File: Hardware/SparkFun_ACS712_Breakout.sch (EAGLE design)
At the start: 12 parts, among them U1 ACS712

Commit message: A few more QC clean ups
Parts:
- added U$1: REVISION, SparkFun-Aesthetics:REVISION
- JP1, JP2: value M01-SMTSO-256-ET -> (none); device SparkFun:M01-SMTSO-256-ET -> SparkFun-Connectors:M01-SMTSO-256-ET
- JP3: device SparkFun:M04PTH -> SparkFun-Connectors:M04PTH
- JP4, JP5: device SparkFun:FIDUCIALUFIDUCIAL -> SparkFun-Aesthetics:FIDUCIALUFIDUCIAL
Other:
- note added: "P. Alberts, Toni Klopfenstein"
- note removed: "Revised by:Patrick Alberts"
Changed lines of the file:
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@@
 <?xml version="1.0" encoding="utf-8"?>
 <!DOCTYPE eagle SYSTEM "eagle.dtd">
-<eagle version="7.2.0">
+<eagle version="7.3.0">
 <drawing>
 <settings>
@@
 <layer number="113" name="IDFDebug" color="4" fill="1" visible="yes" active="yes"/>
 <layer number="116" name="Patch_BOT" color="9" fill="4" visible="no" active="yes"/>
+<layer number="118" name="Rect_Pads" color="7" fill="1" visible="yes" active="yes"/>
 <layer number="121" name="_tsilk" color="7" fill="1" visible="no" active="yes"/>
 <layer number="122" name="_bsilk" color="7" fill="1" visible="no" active="yes"/>
@@
 <layer number="255" name="routoute" color="7" fill="1" visible="yes" active="yes"/>
 </layers>
-<schematic xreflabel="%F%N/%S" xrefpart="/%S.%C%R">
+<schematic xreflabel="%F%N/%S" xrefpart="/%S">
 <attributes>
 </attributes>
@@
 <part name="U1" library="SparkFun-AnalogIC" deviceset="ACS712" device=""/>
 <part name="FRAME1" library="SparkFun-Aesthetics" deviceset="FRAME-LETTER" device=""/>
-<part name="JP1" library="SparkFun" deviceset="M01" device="-SMTSO-256-ET"/>
-<part name="JP2" library="SparkFun" deviceset="M01" device="-SMTSO-256-ET"/>
-<part name="JP3" library="SparkFun" deviceset="M04" device="PTH"/>
+<part name="JP1" library="SparkFun-Connectors" deviceset="M01" device="-SMTSO-256-ET"/>
+<part name="JP2" library="SparkFun-Connectors" deviceset="M01" device="-SMTSO-256-ET"/>
+<part name="JP3" library="SparkFun-Connectors" deviceset="M04" device="PTH"/>
 <part name="U$3" library="SparkFun" deviceset="OSHW-LOGO" device="S"/>
-<part name="JP4" library="SparkFun" deviceset="FIDUCIAL" device="UFIDUCIAL"/>
-<part name="JP5" library="SparkFun" deviceset="FIDUCIAL" device="UFIDUCIAL"/>
+<part name="JP4" library="SparkFun-Aesthetics" deviceset="FIDUCIAL" device="UFIDUCIAL"/>
+<part name="JP5" library="SparkFun-Aesthetics" deviceset="FIDUCIAL" device="UFIDUCIAL"/>
 <part name="JP6" library="SparkFun-Connectors" deviceset="M02" device="1X02_NO_SILK"/>
 <part name="LOGO2" library="SparkFun-Aesthetics" deviceset="SFE_LOGO_FLAME" device=".3_INCH"/>
@@
 <part name="GND1" library="SparkFun-Aesthetics" deviceset="GND" device=""/>
 <part name="GND2" library="SparkFun-Aesthetics" deviceset="GND" device=""/>
+<part name="U$1" library="SparkFun-Aesthetics" deviceset="REVISION" device=""/>
 </parts>
 <sheets>
@@
 <plain>
 <text x="170.18" y="11.43" size="2.54" layer="94">Pete Dokter</text>
-<text x="148.59" y="6.858" size="2.54" layer="94">Revised by:Patrick Alberts</text>
 <text x="236.982" y="7.366" size="2.54" layer="94">V12</text>
 <text x="147.828" y="115.824" size="1.905" layer="97" font="vector" ratio="10">5VDC</text>
+<text x="175.768" y="6.858" size="2.54" layer="94">P. Alberts, Toni Klopfenstein</text>
 </plain>
 <instances>
@@
 <instance part="GND1" gate="1" x="144.78" y="83.82"/>
 <instance part="GND2" gate="1" x="157.48" y="83.82"/>
+<instance part="U$1" gate="G$1" x="149.098" y="6.858"/>
 </instances>
 <busses>

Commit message: Silk fix
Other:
- note added: "Max Current Sensing: 5A"
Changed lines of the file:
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@@
 <text x="147.828" y="115.824" size="1.905" layer="97" font="vector" ratio="10">5VDC</text>
 <text x="175.768" y="6.858" size="2.54" layer="94">P. Alberts, Toni Klopfenstein</text>
+<text x="109.22" y="127" size="1.778" layer="97">Max Current Sensing: 5A</text>
 </plain>
 <instances>

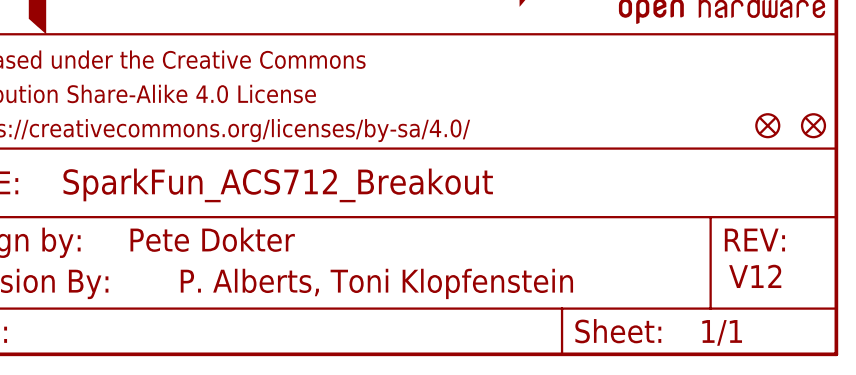
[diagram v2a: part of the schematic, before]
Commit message: Adding second trace on bottom layer
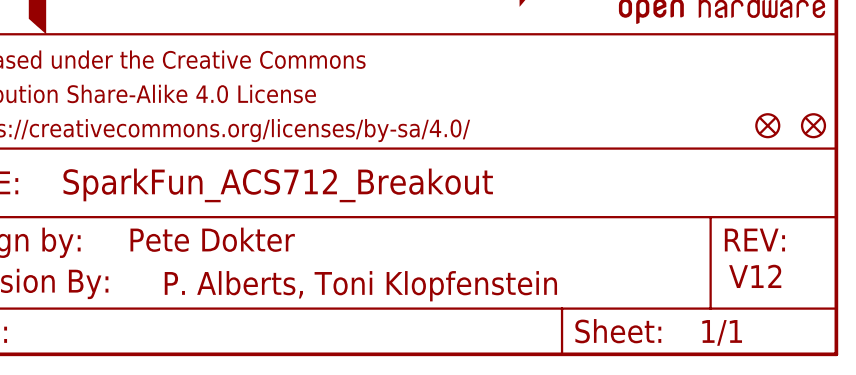
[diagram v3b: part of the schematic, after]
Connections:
- net N$1 renamed IP+
- net N$3 renamed IP-
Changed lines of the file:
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@@
 <text x="236.982" y="7.366" size="2.54" layer="94">V12</text>
 <text x="147.828" y="115.824" size="1.905" layer="97" font="vector" ratio="10">5VDC</text>
-<text x="175.768" y="6.858" size="2.54" layer="94">P. Alberts, Toni Klopfenstein</text>
+<text x="173.99" y="6.604" size="2.54" layer="94">P. Alberts, Toni Klopfenstein</text>
 <text x="109.22" y="127" size="1.778" layer="97">Max Current Sensing: 5A</text>
 </plain>
@@
 </busses>
 <nets>
-<net name="N$1" class="0">
+<net name="IP+" class="0">
 <segment>
 <wire x1="93.98" y1="116.84" x2="104.14" y2="116.84" width="0.1524" layer="91"/>
@@
 </segment>
 </net>
-<net name="N$3" class="0">
+<net name="IP-" class="0">
 <segment>
 <wire x1="109.22" y1="101.6" x2="104.14" y2="101.6" width="0.1524" layer="91"/>
